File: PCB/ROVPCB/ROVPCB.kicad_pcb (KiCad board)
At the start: 2 copper layers, 65 x 56 mm, 7 parts, among them J1 Conn_01x04_Male, J2 Conn_01x04_Male, P1 Conn_02x20_Odd_Even

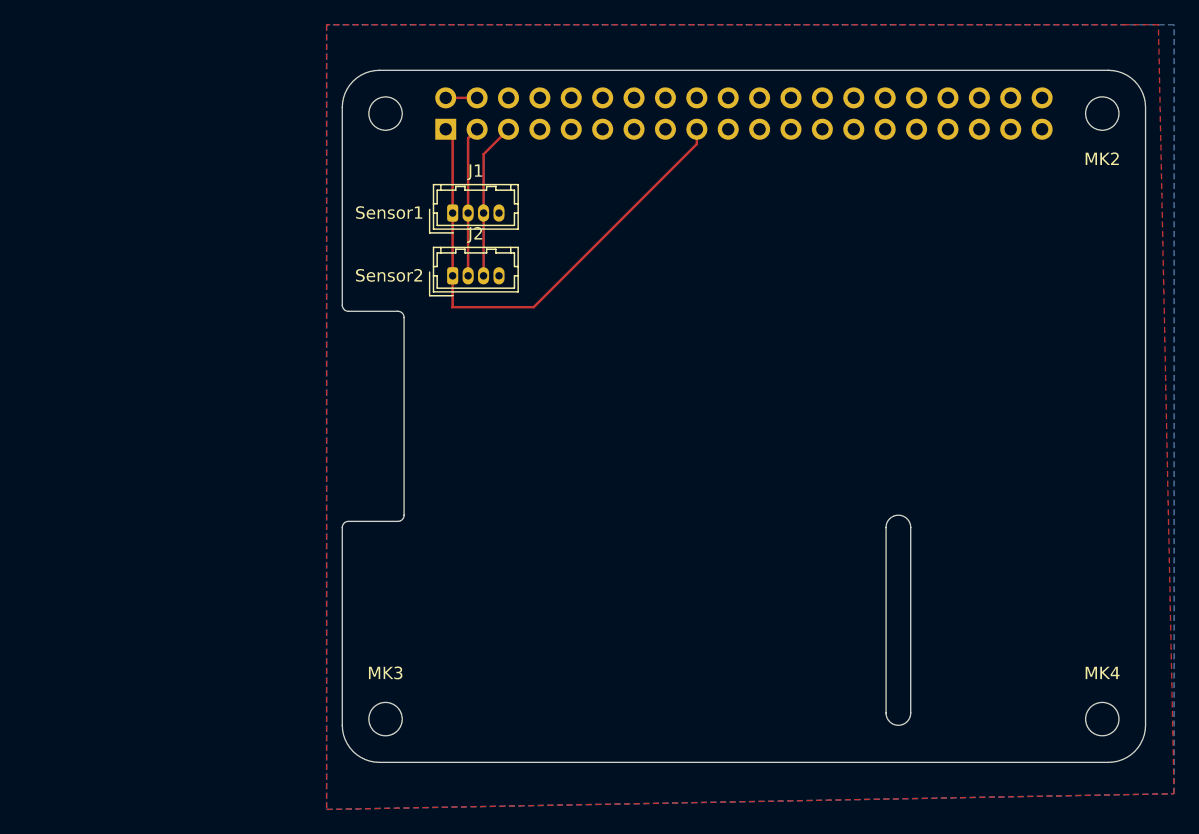
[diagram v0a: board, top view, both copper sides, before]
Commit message: Small Changes to pcb to make it look nice.
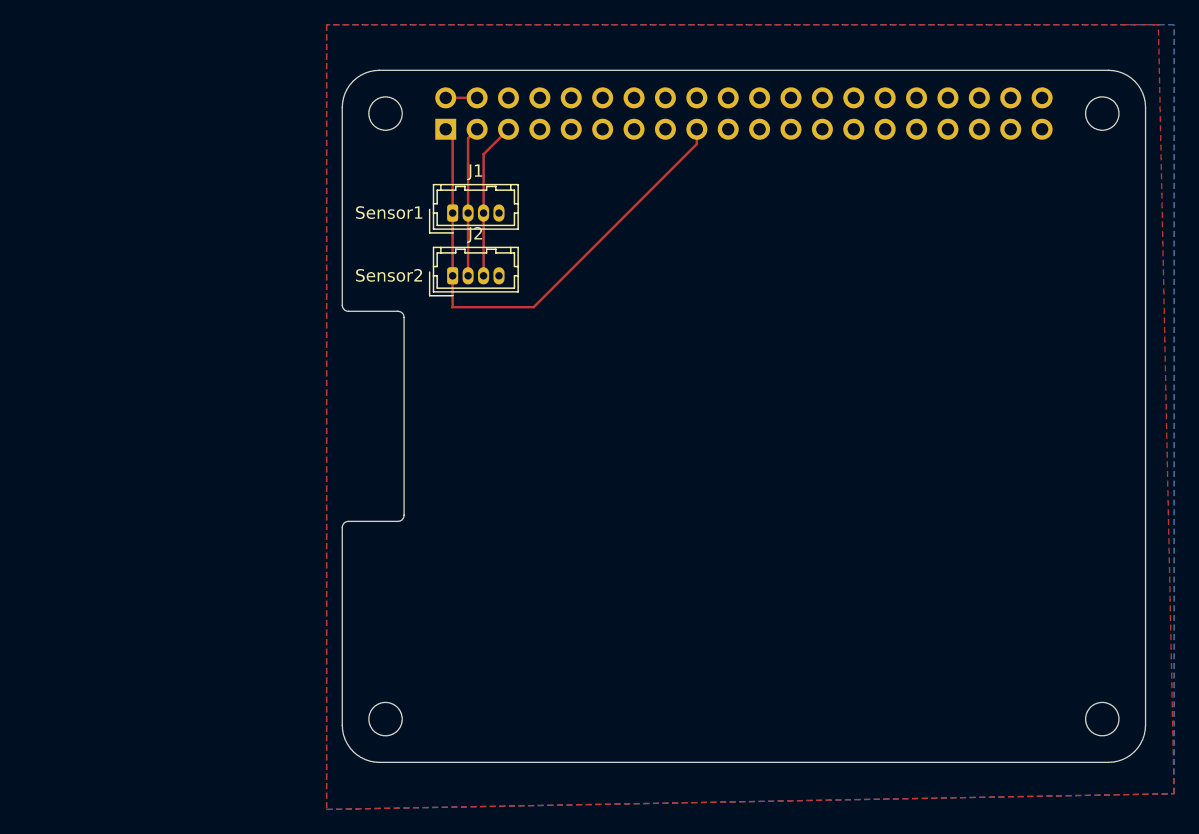
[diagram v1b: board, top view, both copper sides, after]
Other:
- outline, holes or cut-outs redrawn
- board text removed: "CAMERA"
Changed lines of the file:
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@@
   (general
     (thickness 1.6)
-    (drawings 41)
+    (drawings 36)
     (tracks 15)
     (zones 0)
@@
     (tags "mounting hole 2.7mm no annular m2.5")
     (attr virtual)
-    (fp_text reference MK4 (at 0 -3.7) (layer F.SilkS)
+    (fp_text reference MK4 (at 0 -3.7) (layer F.SilkS) hide
       (effects (font (size 1 1) (thickness 0.15)))
     )
@@
     (tags "mounting hole 2.7mm no annular m2.5")
     (attr virtual)
-    (fp_text reference MK3 (at 0 -3.7) (layer F.SilkS)
+    (fp_text reference MK3 (at 0 -3.7) (layer F.SilkS) hide
       (effects (font (size 1 1) (thickness 0.15)))
     )
@@
     (tags "mounting hole 2.7mm no annular m2.5")
     (attr virtual)
-    (fp_text reference MK2 (at 0 -3.7 180) (layer F.SilkS)
+    (fp_text reference MK2 (at 0 -3.7 180) (layer F.SilkS) hide
       (effects (font (size 1 1) (thickness 0.15)))
     )
@@
     (effects (font (size 1 1) (thickness 0.25)))
   )
-  (gr_line (start 244 146) (end 244 131) (layer Edge.Cuts) (width 0.1))
-  (gr_line (start 246 131) (end 246 146) (layer Edge.Cuts) (width 0.1))
-  (gr_arc (start 245 131) (end 244 131) (angle 180) (layer Edge.Cuts) (width 0.1))
-  (gr_arc (start 245 146) (end 246 146) (angle 180) (layer Edge.Cuts) (width 0.1))
   (gr_arc (start 200.5 131) (end 200 131) (angle 89.9) (layer Edge.Cuts) (width 0.1))
   (gr_arc (start 204.5 130) (end 205 130) (angle 90) (layer Edge.Cuts) (width 0.1))
@@
   (gr_line (start 200 97) (end 200 113) (layer Edge.Cuts) (width 0.1))
   (gr_text DISPLAY (at 202.5 122 90) (layer Dwgs.User)
-    (effects (font (size 1 1) (thickness 0.15)))
-  )
-  (gr_text CAMERA (at 245 139 90) (layer Dwgs.User)
     (effects (font (size 1 1) (thickness 0.15)))
   )
@@
     (connect_pads (clearance 0.508))
     (min_thickness 0.254)
-    (fill (arc_segments 16) (thermal_gap 0.508) (thermal_bridge_width 0.508))
+    (fill yes (arc_segments 16) (thermal_gap 0.508) (thermal_bridge_width 0.508))
     (polygon
       (pts
@@
     (connect_pads (clearance 0.508))
     (min_thickness 0.254)
-    (fill (arc_segments 16) (thermal_gap 0.508) (thermal_bridge_width 0.508))
+    (fill yes (arc_segments 16) (thermal_gap 0.508) (thermal_bridge_width 0.508))
     (polygon
       (pts

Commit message: Added Accelerometer to schematic and Board.
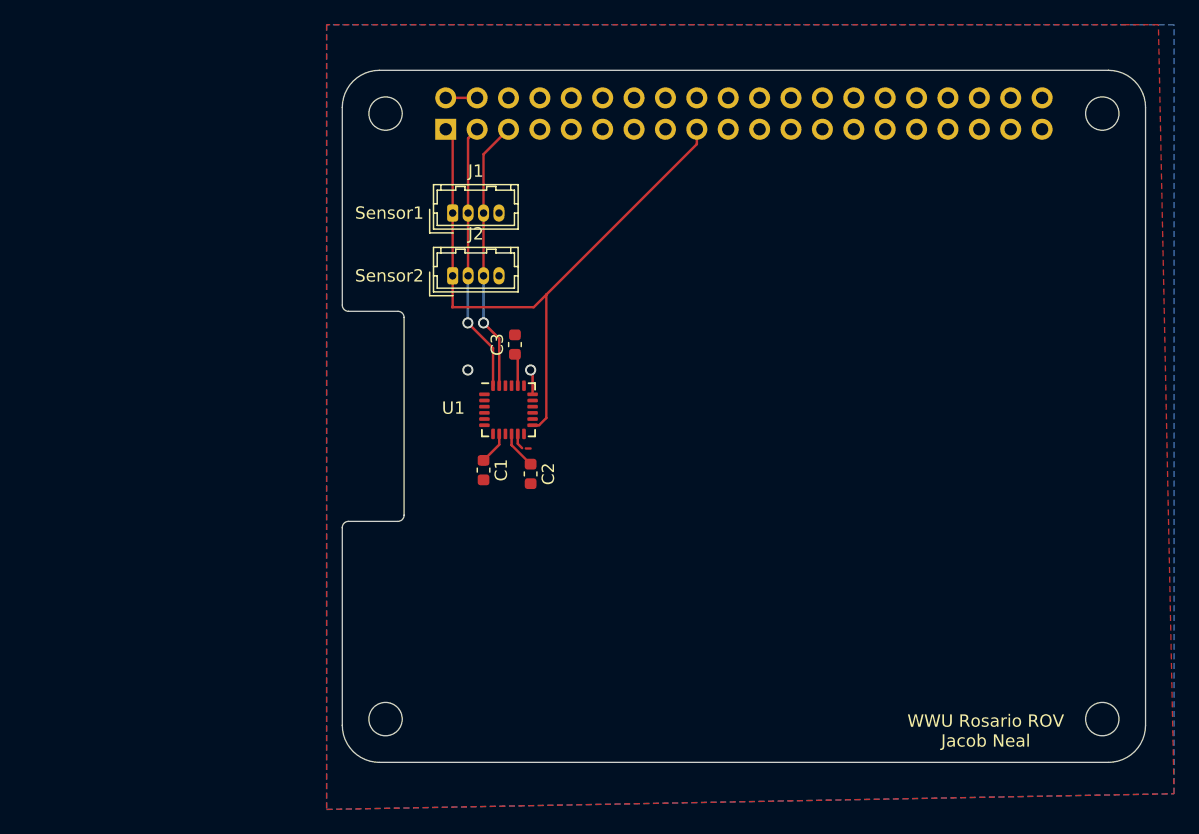
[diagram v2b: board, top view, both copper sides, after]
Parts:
- added C1: 10nF, Capacitor_SMD:C_0603_1608Metric, F.Cu at (211.4, 126.4)
- added C2: 0.1uF, Capacitor_SMD:C_0603_1608Metric, F.Cu at (215.2, 126.7)
- added C3: 2.2 nF, Capacitor_SMD:C_0603_1608Metric, F.Cu at (214.0, 116.2)
- added U1: MPU-6050, Sensor_Motion:InvenSense_QFN-24_4x4mm_P0.5mm, F.Cu at (213.4, 121.5)
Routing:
- net +3V3: track 41.1 -> 52.5 mm
- net /GPIO2(SDA1): track 12.2 -> 21.9 mm, vias 0 -> 1
- net /GPIO3(SCL1): track 12.7 -> 22.1 mm, vias 0 -> 1
- net GND: track 0.00 -> 3.49 mm, vias 0 -> 2
- net Net-(C2-Pad1): track 0.00 -> 3.09 mm
- net Net-(C1-Pad1): track 0.00 -> 2.67 mm
- net Net-(C3-Pad1): track 0.00 -> 2.64 mm
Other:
- board text added: "WWU Rosario ROV Jacob Neal"

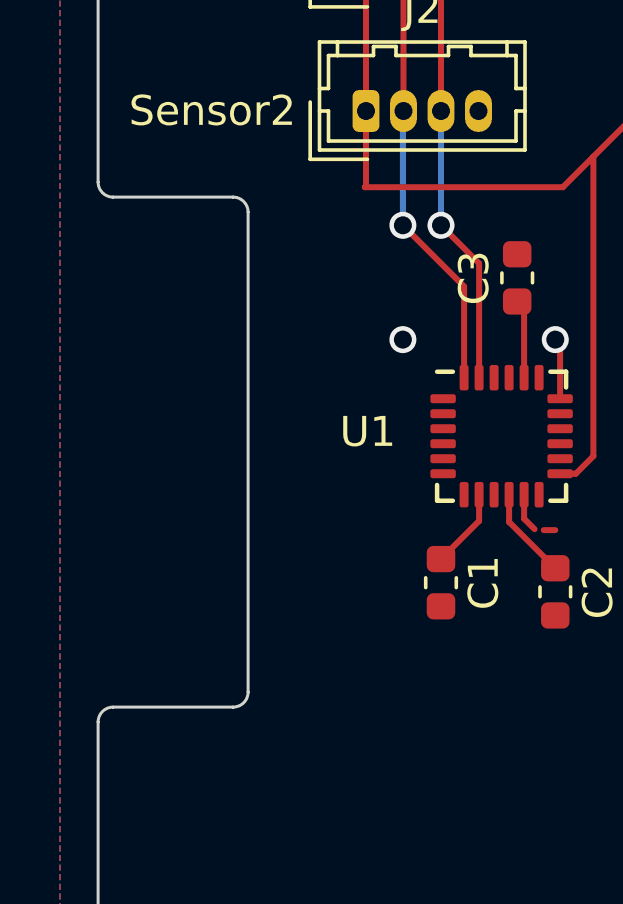
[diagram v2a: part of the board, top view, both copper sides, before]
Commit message: Filling in Display cutout on PCB
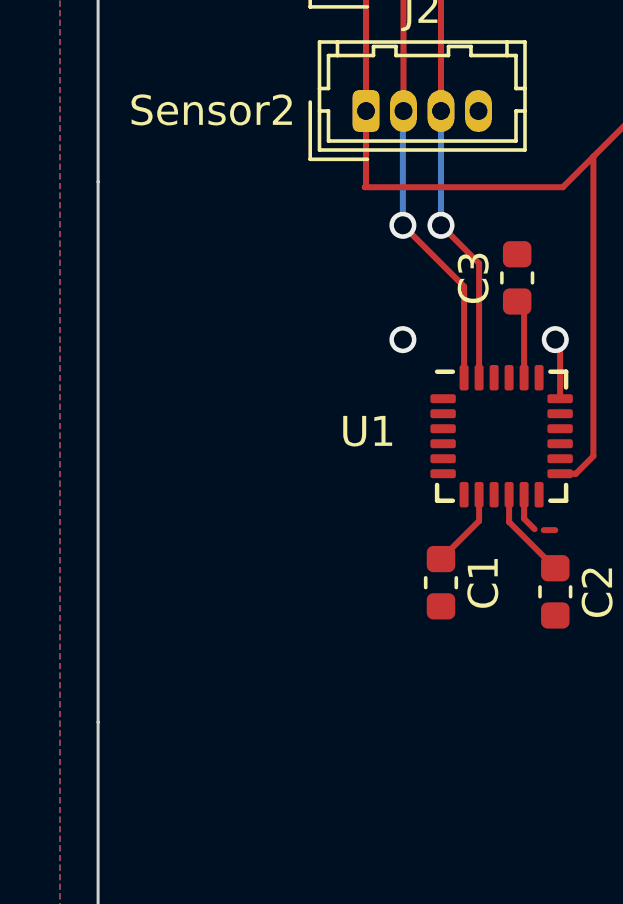
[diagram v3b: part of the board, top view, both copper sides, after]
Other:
- outline, holes or cut-outs redrawn
- board text removed: "DISPLAY"
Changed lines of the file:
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@@
   (general
     (thickness 1.6)
-    (drawings 37)
+    (drawings 29)
     (tracks 40)
     (zones 0)
@@
     )
   )
-  (gr_line (start 205 114) (end 205 130) (layer Edge.Cuts) (width 0.1))
+  (gr_line (start 200 112.9795) (end 200 131.0135) (layer Edge.Cuts) (width 0.1))
   (gr_text "WWU Rosario ROV\nJacob Neal" (at 252.07 147.46) (layer F.SilkS)
     (effects (font (size 1 1) (thickness 0.25)))
@@
     (effects (font (size 1 1) (thickness 0.25)))
   )
-  (gr_arc (start 200.5 131) (end 200 131) (angle 89.9) (layer Edge.Cuts) (width 0.1))
-  (gr_arc (start 204.5 130) (end 205 130) (angle 90) (layer Edge.Cuts) (width 0.1))
-  (gr_arc (start 200.5 113) (end 200.5 113.5) (angle 90) (layer Edge.Cuts) (width 0.1))
-  (gr_arc (start 204.5 114) (end 204.5 113.5) (angle 90) (layer Edge.Cuts) (width 0.1))
-  (gr_line (start 200 113) (end 200 131) (layer Dwgs.User) (width 0.1))
   (gr_line (start 200 97) (end 200 113) (layer Edge.Cuts) (width 0.1))
-  (gr_text DISPLAY (at 202.5 122 90) (layer Dwgs.User)
-    (effects (font (size 1 1) (thickness 0.15)))
-  )
   (gr_text RJ45 (at 276.2 139.84) (layer Dwgs.User)
     (effects (font (size 2 2) (thickness 0.15)))
@@
   (gr_line (start 287 127.55) (end 269.9 127.55) (layer Dwgs.User) (width 0.1))
   (gr_line (start 287 114.45) (end 287 127.55) (layer Dwgs.User) (width 0.1))
-  (gr_line (start 204.5 130.5) (end 200.5 130.5) (layer Edge.Cuts) (width 0.1))
-  (gr_line (start 200.5 113.5) (end 204.5 113.5) (layer Edge.Cuts) (width 0.1))
   (gr_line (start 266 147.675) (end 266 131.825) (layer Dwgs.User) (width 0.1))
   (gr_line (start 287 147.675) (end 266 147.675) (layer Dwgs.User) (width 0.1))

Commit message: Added all the things
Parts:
- added R1: 10k, Resistor_SMD:R_0805_2012Metric, F.Cu at (244.4, 123.3)
- added U2: BME280, Package_LGA:Bosch_LGA-8_2.5x2.5mm_P0.65mm_ClockwisePinNumbering, F.Cu at (247.8, 121.4)
- added U3: LIGHT_TSL2591, Adafruit TSL2591:DFN6_TAOS, F.Cu at (244.9, 121.2)
- C1: value 10nF -> 0.1uF
- C3: value 2.2 nF -> 0.1uF
- U1: value MPU-6050 -> MPU-9250
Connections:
- C2 pad 1: Net-(C2-Pad1) -> +3V3
- C3 pad 1: Net-(C3-Pad1) -> +3V3
- U1 pad 1: GND -> +3V3
- U1 pad 10: Net-(C2-Pad1) -> Net-(C1-Pad1)
- U1 pad 20: Net-(C3-Pad1) -> GND
- U1 pad 21: (no net) -> Net-(U1-Pad21)
- U1 pad 22: (no net) -> +3V3
- U1 pad 6: Net-(U1-Pad6) -> (no net)
- U1 pad 8: Net-(C1-Pad1) -> +3V3
- U1 pad 9: GND -> Net-(R1-Pad1)

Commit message: HouseKeepinggit add *
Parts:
- added U4: LTC4316IDDPBF, LTC4316IDDPBF:DFN-10_DD, F.Cu at (250.3, 114.5)
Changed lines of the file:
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@@
     (tracks 40)
     (zones 0)
-    (modules 14)
-    (nets 41)
+    (modules 15)
+    (nets 52)
   )
   (page A3)
@@
   (net 39 "Net-(U3-Pad2)")
   (net 40 "Net-(U3-Pad4)")
+  (net 41 "Net-(U4-Pad1)")
+  (net 42 "Net-(U4-Pad2)")
+  (net 43 "Net-(U4-Pad3)")
+  (net 44 "Net-(U4-Pad4)")
+  (net 45 "Net-(U4-Pad5)")
+  (net 46 "Net-(U4-Pad6)")
+  (net 47 "Net-(U4-Pad7)")
+  (net 48 "Net-(U4-Pad8)")
+  (net 49 "Net-(U4-Pad9)")
+  (net 50 "Net-(U4-Pad10)")
+  (net 51 "Net-(U4-Pad11)")
   (net_class Default "This is the default net class."
     (clearance 0.2)
@@
     (add_net "Net-(U3-Pad2)")
     (add_net "Net-(U3-Pad4)")
+    (add_net "Net-(U4-Pad1)")
+    (add_net "Net-(U4-Pad10)")
+    (add_net "Net-(U4-Pad11)")
+    (add_net "Net-(U4-Pad2)")
+    (add_net "Net-(U4-Pad3)")
+    (add_net "Net-(U4-Pad4)")
+    (add_net "Net-(U4-Pad5)")
+    (add_net "Net-(U4-Pad6)")
+    (add_net "Net-(U4-Pad7)")
+    (add_net "Net-(U4-Pad8)")
+    (add_net "Net-(U4-Pad9)")
   )
   (net_class Power ""
@@
       (net 9 "/GPIO2(SDA1)") (solder_mask_margin 0.0508))
   )
+  (module LTC4316IDDPBF:DFN-10_DD (layer F.Cu)
+    (at 250.34 114.47)
+    (attr smd)
+    (fp_text reference U4 (at -1.0542 -2.0524) (layer F.SilkS)
+      (effects (font (size 0.314961 0.314961) (thickness 0.05)))
+    )
+    (fp_text value LTC4316IDDPBF (at -0.8542 2.0524) (layer F.SilkS)
+      (effects (font (size 0.314961 0.314961) (thickness 0.05)))
+    )
+    (fp_poly (pts (xy -0.8763 -1.2446) (xy -0.8763 1.2446) (xy 0.8763 1.2446) (xy 0.8763 -1.2446)) (layer F.Paste) (width 0.0254))
+    (fp_line (start -1.6764 1.6764) (end 1.6764 1.6764) (layer F.SilkS) (width 0.1524))
+    (fp_line (start 1.6764 -1.6764) (end -1.6764 -1.6764) (layer F.SilkS) (width 0.1524))
+    (fp_line (start -1.5494 1.5494) (end 1.5494 1.5494) (layer Eco2.User) (width 0.1524))
+    (fp_line (start 1.5494 1.5494) (end 1.5494 -1.5494) (layer Eco2.User) (width 0.1524))
+    (fp_line (start 1.5494 -1.5494) (end 0.3048 -1.5494) (layer Eco2.User) (width 0.1524))
+    (fp_line (start 0.3048 -1.5494) (end -0.3048 -1.5494) (layer Eco2.User) (width 0.1524))
+    (fp_line (start -0.3048 -1.5494) (end -1.5494 -1.5494) (layer Eco2.User) (width 0.1524))
+    (fp_line (start -1.5494 -1.5494) (end -1.5494 1.5494) (layer Eco2.User) (width 0.1524))
+    (fp_arc (start 0 -1.5494) (end -0.3048 -1.5494) (angle -180) (layer Eco2.User) (width 0.1524))
+    (pad 1 smd rect (at -1.4478 -1) (size 0.8128 0.3048) (layers F.Cu F.Paste F.Mask)
+      (net 41 "Net-(U4-Pad1)"))
+    (pad 2 smd rect (at -1.4478 -0.5) (size 0.8128 0.3048) (layers F.Cu F.Paste F.Mask)
+      (net 42 "Net-(U4-Pad2)"))
+    (pad 3 smd rect (at -1.4478 0) (size 0.8128 0.3048) (layers F.Cu F.Paste F.Mask)
+      (net 43 "Net-(U4-Pad3)"))
+    (pad 4 smd rect (at -1.4478 0.5) (size 0.8128 0.3048) (layers F.Cu F.Paste F.Mask)
+      (net 44 "Net-(U4-Pad4)"))
+    (pad 5 smd rect (at -1.4478 1) (size 0.8128 0.3048) (layers F.Cu F.Paste F.Mask)
+      (net 45 "Net-(U4-Pad5)"))
+    (pad 6 smd rect (at 1.4478 1) (size 0.8128 0.3048) (layers F.Cu F.Paste F.Mask)
+      (net 46 "Net-(U4-Pad6)"))
+    (pad 7 smd rect (at 1.4478 0.5) (size 0.8128 0.3048) (layers F.Cu F.Paste F.Mask)
+      (net 47 "Net-(U4-Pad7)"))
+    (pad 8 smd rect (at 1.4478 0) (size 0.8128 0.3048) (layers F.Cu F.Paste F.Mask)
+      (net 48 "Net-(U4-Pad8)"))
+    (pad 9 smd rect (at 1.4478 -0.5) (size 0.8128 0.3048) (layers F.Cu F.Paste F.Mask)
+      (net 49 "Net-(U4-Pad9)"))
+    (pad 10 smd rect (at 1.4478 -1) (size 0.8128 0.3048) (layers F.Cu F.Paste F.Mask)
+      (net 50 "Net-(U4-Pad10)"))
+    (pad 11 smd rect (at 0 0) (size 1.7526 2.4892) (layers F.Cu F.Paste F.Mask)
+      (net 51 "Net-(U4-Pad11)"))
+  )
   (gr_line (start 200 112.9795) (end 200 131.0135) (layer Edge.Cuts) (width 0.1))

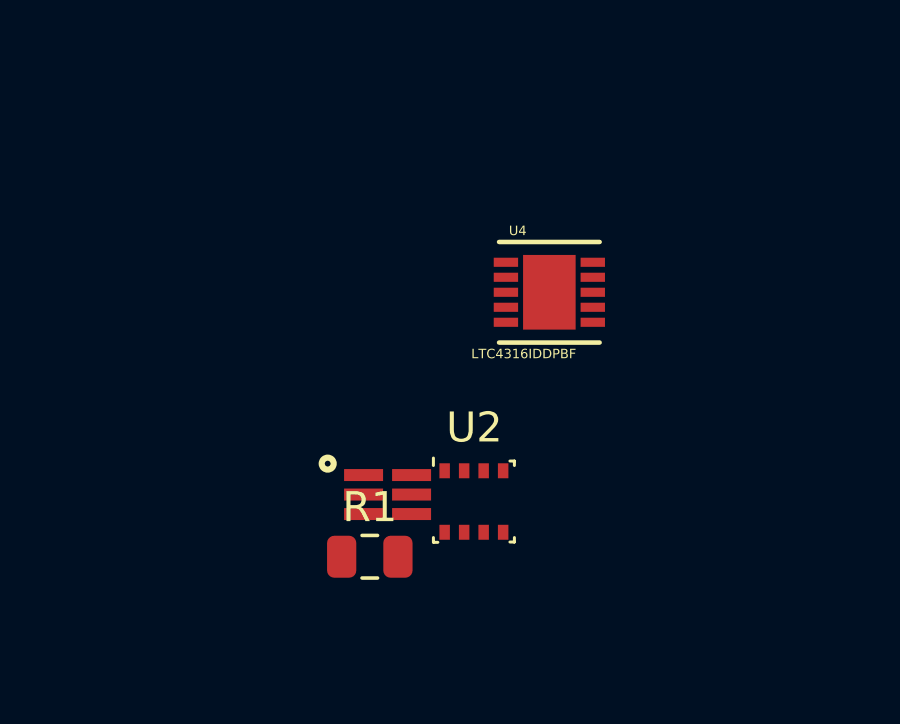
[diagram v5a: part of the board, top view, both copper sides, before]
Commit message: Added I2C Address Translator
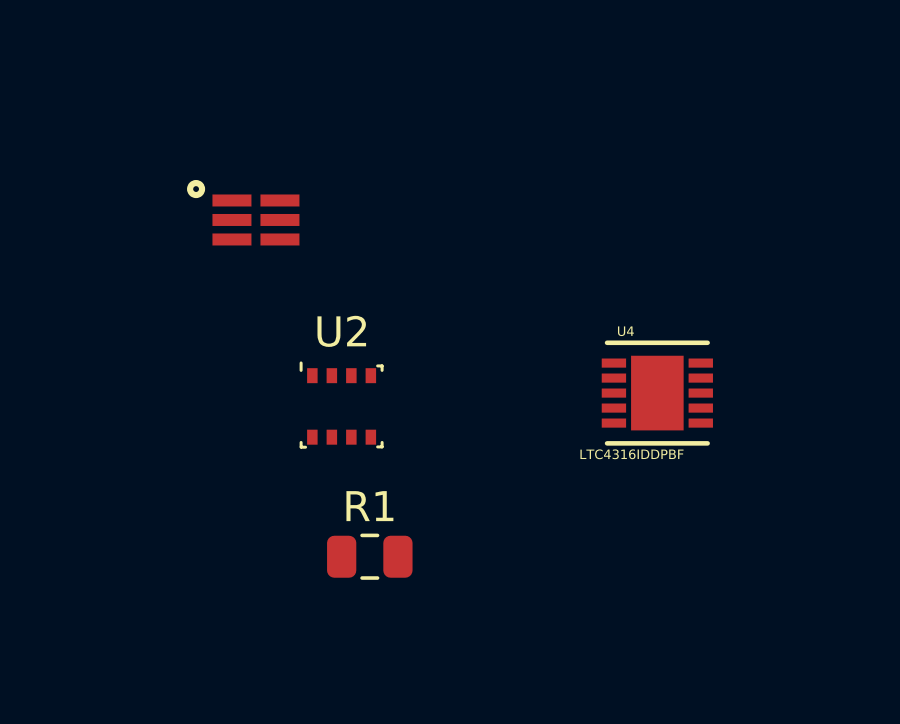
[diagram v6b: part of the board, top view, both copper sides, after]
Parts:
- moved U3 10.1 mm to (240.6, 112.1)
- moved U2 5.43 mm to (243.4, 118.3)
- moved U4 4.92 mm to (253.9, 117.8)
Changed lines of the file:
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@@
   )
   (module Package_LGA:Bosch_LGA-8_2.5x2.5mm_P0.65mm_ClockwisePinNumbering (layer F.Cu)
-    (at 247.825001 121.445001)
+    (at 243.415 118.275)
     (descr LGA-8)
     (tags "lga land grid array")
@@
   )
   (module "Adafruit TSL2591:DFN6_TAOS" (layer F.Cu)
-    (at 244.947601 121.212601)
+    (at 240.56 112.06)
     (fp_text reference U3 (at 0 0) (layer F.SilkS) hide
       (effects (font (size 1.27 1.27) (thickness 0.15)) (justify right top))
@@
   )
   (module LTC4316IDDPBF:DFN-10_DD (layer F.Cu)
-    (at 250.34 114.47)
+    (at 253.94 117.83)
     (attr smd)
     (fp_text reference U4 (at -1.0542 -2.0524) (layer F.SilkS)
